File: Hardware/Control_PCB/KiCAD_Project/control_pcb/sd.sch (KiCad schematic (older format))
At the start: 9 parts, among them J5 Micro_SD_Card_Det

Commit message: Draft of next layout
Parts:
- added C12, C13, C14, C15: 1-0000007, capacitors_0603:1-0000007, symbol capacitors_0603:1-0000007
- added D6: Activity, LED_SMD:LED_0805_2012Metric, symbol Device:LED
- added D7: Error, LED_SMD:LED_0805_2012Metric, symbol Device:LED
- added J7: SD_uC_ISP, Connector_PinHeader_2.54mm:PinHeader_2x03_P2.54mm_Vertical, symbol Connector_Generic:Conn_02x03_Odd_Even
- added R25: 1-0000010, resistors_0603:1-0000010, symbol resistors_0603:1-0000010
- added R26, R27: 1-0000006, resistors_0603:1-0000006, symbol resistors_0603:1-0000006
- added R28, R36: 150, Resistor_SMD:R_0603_1608Metric, symbol Device:R
- added U4: ATmega328P-AU, Package_QFP:TQFP-32_7x7mm_P0.8mm, symbol lib_sch:ATmega328P-AU
- added Y3: 16MHz, lib_fp:Resonator, symbol Device:Resonator_Small
- C16: renamed from C11; footprint Capacitors_SMD:C_0603_HandSoldering -> Capacitor_SMD:C_0603_1608Metric
- R29: renamed from R11; footprint Resistors_SMD:R_0603_HandSoldering -> Resistor_SMD:R_0603_1608Metric
- R30: renamed from R12; footprint Resistors_SMD:R_0603_HandSoldering -> Resistor_SMD:R_0603_1608Metric
- R31: renamed from R13; footprint Resistors_SMD:R_0603_HandSoldering -> Resistor_SMD:R_0603_1608Metric
- R32: renamed from R14; footprint Resistors_SMD:R_0603_HandSoldering -> Resistor_SMD:R_0603_1608Metric
- R33: renamed from R15; footprint Resistors_SMD:R_0603_HandSoldering -> Resistor_SMD:R_0603_1608Metric
- R34: renamed from R16; footprint Resistors_SMD:R_0603_HandSoldering -> Resistor_SMD:R_0603_1608Metric
- R35: renamed from R17; footprint Resistors_SMD:R_0603_HandSoldering -> Resistor_SMD:R_0603_1608Metric
- renumbered J5 to J6
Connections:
- net +3V3: now also C12.1, C13.1, C14.1, J7.2 (Pin_2), R25.1, U4.18 (AVCC), U4.4 (VCC), U4.6 (VCC)
- net GND: now also C12.2, C13.2, C14.2, C15.2, D6.1 (K), D7.1 (K), J7.6 (Pin_6), U4.21 (GND), U4.3 (GND), U4.5 (GND), Y3.2
- net SD_CS renamed SD_uC_CS
- net SD_uC_CS: now also U4.12 (PB0)
- net SD_DETECT renamed SD_uC_CD
- net SD_uC_CD: now also U4.13 (PB1)
- net SPI1_MISO renamed SD_uC_MISO
- net SD_uC_MISO: now also J7.1 (Pin_1), U4.16 (PB4)
- net SPI1_MOSI renamed SD_uC_MOSI
- net SD_uC_MOSI: now also J7.4 (Pin_4), U4.15 (PB3)
- net SPI1_SCLK renamed SD_uC_SCK
- net SD_uC_SCK: now also J7.3 (Pin_3), U4.17 (PB5)
- new net: R28.2, U4.2 (PD4)
- new net: C15.1, U4.20 (AREF)
- new net: R26.2, U4.30 (PD0)
- new net: R27.2, U4.31 (PD1)
- new net: U4.7 (XTAL1/PB6), Y3.1
- new net: U4.8 (XTAL2/PB7), Y3.3
- new net: R36.2, U4.9 (PD5)
- new net: D6.2 (A), R28.1
- new net: D7.2 (A), R36.1
- new net RX_FROM_STM: R26.1
- new net SD_uC_RESET: J7.5 (Pin_5), R25.2, U4.29 (~RESET~/PC6)
- new net TX_TO_STM: R27.1
- no-connect marks 0 -> 13
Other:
- note added: "SD uC gets the serial data stream from the STM32 and writes it all to the SD card.\nIt handles rolling the file name to the next available and then simply dumps\neverything it receives which should only be complete packets since the STM32\ntakes care of that."
- moved on the sheet: C16, J6, R29, R30, R31, R32, R33, R34, R35

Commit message: Add final production files
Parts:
- J7: Internal Part Number (none) -> 0-0000000; Populated (none) -> 0
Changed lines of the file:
@@
 Sheet 3 6
 Title "Control Paddle Electronics - NSSL EFM"
-Date "2020-03-31"
-Rev "2.0"
+Date "2020-12-30"
+Rev "3.0"
 Comp "Leeman Geophysical LLC"
 Comment1 "(479) 373-3736"
@@
 $EndComp
 $Comp
-L power:+3V3 #PWR041
+L power:+3V3 #PWR039
 U 1 1 5DEE2763
 P 8000 4375
-F 0 "#PWR041" H 8000 4225 50  0001 C CNN
+F 0 "#PWR039" H 8000 4225 50  0001 C CNN
 F 1 "+3V3" H 8015 4548 50  0000 C CNN
 F 2 "" H 8000 4375 50  0001 C CNN
@@
 	8000 5725 8000 4775
 $Comp
-L power:GND #PWR047
+L power:GND #PWR045
 U 1 1 5DEE6EC1
 P 9300 6225
-F 0 "#PWR047" H 9300 5975 50  0001 C CNN
+F 0 "#PWR045" H 9300 5975 50  0001 C CNN
 F 1 "GND" H 9305 6052 50  0000 C CNN
 F 2 "" H 9300 6225 50  0001 C CNN
@@
 $EndComp
 $Comp
-L power:GND #PWR048
+L power:GND #PWR046
 U 1 1 5DEE73D1
 P 9650 6225
-F 0 "#PWR048" H 9650 5975 50  0001 C CNN
+F 0 "#PWR046" H 9650 5975 50  0001 C CNN
 F 1 "GND" H 9655 6052 50  0000 C CNN
 F 2 "" H 9650 6225 50  0001 C CNN
@@
 $EndComp
 $Comp
-L power:GND #PWR042
+L power:GND #PWR040
 U 1 1 5DEEA7AB
 P 9600 4400
-F 0 "#PWR042" H 9600 4150 50  0001 C CNN
+F 0 "#PWR040" H 9600 4150 50  0001 C CNN
 F 1 "GND" H 9605 4227 50  0000 C CNN
 F 2 "" H 9600 4400 50  0001 C CNN
@@
 $EndComp
 $Comp
-L power:+3V3 #PWR040
+L power:+3V3 #PWR038
 U 1 1 5DEEACAB
 P 9300 4275
-F 0 "#PWR040" H 9300 4125 50  0001 C CNN
+F 0 "#PWR038" H 9300 4125 50  0001 C CNN
 F 1 "+3V3" H 9315 4448 50  0000 C CNN
 F 2 "" H 9300 4275 50  0001 C CNN
@@
 P 2925 3175
 AR Path="/5DED0CD0/5FF2D775" Ref="#PWR?"  Part="1"
-AR Path="/5DEDFC42/5FF2D775" Ref="#PWR039"  Part="1"
-F 0 "#PWR039" H 2925 2925 50  0001 C CNN
+AR Path="/5DEDFC42/5FF2D775" Ref="#PWR037"  Part="1"
+F 0 "#PWR037" H 2925 2925 50  0001 C CNN
 F 1 "GND" H 2930 3002 50  0000 C CNN
 F 2 "" H 2925 3175 50  0001 C CNN
@@
 P 3975 5275
 AR Path="/5DED0CD0/5FF2D793" Ref="#PWR?"  Part="1"
-AR Path="/5DEDFC42/5FF2D793" Ref="#PWR044"  Part="1"
-F 0 "#PWR044" H 3975 5025 50  0001 C CNN
+AR Path="/5DEDFC42/5FF2D793" Ref="#PWR042"  Part="1"
+F 0 "#PWR042" H 3975 5025 50  0001 C CNN
 F 1 "GND" H 3980 5102 50  0000 C CNN
 F 2 "" H 3975 5275 50  0001 C CNN
@@
 P 3075 2475
 AR Path="/5DED0CD0/5FF2D7A9" Ref="#PWR?"  Part="1"
-AR Path="/5DEDFC42/5FF2D7A9" Ref="#PWR038"  Part="1"
-F 0 "#PWR038" H 3075 2225 50  0001 C CNN
+AR Path="/5DEDFC42/5FF2D7A9" Ref="#PWR036"  Part="1"
+F 0 "#PWR036" H 3075 2225 50  0001 C CNN
 F 1 "GND" H 3080 2302 50  0000 C CNN
 F 2 "" H 3075 2475 50  0001 C CNN
@@
 P 3975 1375
 AR Path="/5DED0CD0/5FF2D7E6" Ref="#PWR?"  Part="1"
-AR Path="/5DEDFC42/5FF2D7E6" Ref="#PWR035"  Part="1"
-F 0 "#PWR035" H 3975 1225 50  0001 C CNN
+AR Path="/5DEDFC42/5FF2D7E6" Ref="#PWR033"  Part="1"
+F 0 "#PWR033" H 3975 1225 50  0001 C CNN
 F 1 "+3V3" H 3990 1548 50  0000 C CNN
 F 2 "" H 3975 1375 50  0001 C CNN
@@
 P 3250 2025
 AR Path="/5DED0CD0/5FF2D7EC" Ref="#PWR?"  Part="1"
-AR Path="/5DEDFC42/5FF2D7EC" Ref="#PWR036"  Part="1"
-F 0 "#PWR036" H 3250 1775 50  0001 C CNN
+AR Path="/5DEDFC42/5FF2D7EC" Ref="#PWR034"  Part="1"
+F 0 "#PWR034" H 3250 1775 50  0001 C CNN
 F 1 "GND" H 3100 1950 50  0000 C CNN
 F 2 "" H 3250 2025 50  0001 C CNN
@@
 P 2525 2400
 AR Path="/5DED0CD0/5FF2D7FA" Ref="#PWR?"  Part="1"
-AR Path="/5DEDFC42/5FF2D7FA" Ref="#PWR037"  Part="1"
-F 0 "#PWR037" H 2525 2250 50  0001 C CNN
+AR Path="/5DEDFC42/5FF2D7FA" Ref="#PWR035"  Part="1"
+F 0 "#PWR035" H 2525 2250 50  0001 C CNN
 F 1 "+3V3" H 2540 2573 50  0000 C CNN
 F 2 "" H 2525 2400 50  0001 C CNN
@@
 P 4300 5925
 AR Path="/5DED0CD0/5FF2D808" Ref="#PWR?"  Part="1"
-AR Path="/5DEDFC42/5FF2D808" Ref="#PWR045"  Part="1"
-F 0 "#PWR045" H 4300 5775 50  0001 C CNN
+AR Path="/5DEDFC42/5FF2D808" Ref="#PWR043"  Part="1"
+F 0 "#PWR043" H 4300 5775 50  0001 C CNN
 F 1 "+3V3" H 4315 6098 50  0000 C CNN
 F 2 "" H 4300 5925 50  0001 C CNN
@@
 P 4300 6125
 AR Path="/5DED0CD0/5FF2D816" Ref="#PWR?"  Part="1"
-AR Path="/5DEDFC42/5FF2D816" Ref="#PWR046"  Part="1"
-F 0 "#PWR046" H 4300 5875 50  0001 C CNN
+AR Path="/5DEDFC42/5FF2D816" Ref="#PWR044"  Part="1"
+F 0 "#PWR044" H 4300 5875 50  0001 C CNN
 F 1 "GND" H 4305 5952 50  0000 C CNN
 F 2 "" H 4300 6125 50  0001 C CNN
@@
 P 5850 4900
 AR Path="/5FFDD0BF" Ref="#PWR?"  Part="1"
-AR Path="/5DEDFC42/5FFDD0BF" Ref="#PWR043"  Part="1"
-F 0 "#PWR043" H 5850 4650 50  0001 C CNN
+AR Path="/5DEDFC42/5FFDD0BF" Ref="#PWR041"  Part="1"
+F 0 "#PWR041" H 5850 4650 50  0001 C CNN
 F 1 "GND" H 5855 4727 50  0000 C CNN
 F 2 "" H 5850 4900 50  0001 C CNN
@@
 F 2 "Connector_PinHeader_2.54mm:PinHeader_2x03_P2.54mm_Vertical" H 4000 6025 50  0001 C CNN
 F 3 "~" H 4000 6025 50  0001 C CNN
+F 4 "0-0000000" H 4000 6025 50  0001 C CNN "Internal Part Number"
+F 5 "0" H 4000 6025 50  0001 C CNN "Populated"
 	1    4000 6025
 	1    0    0    -1

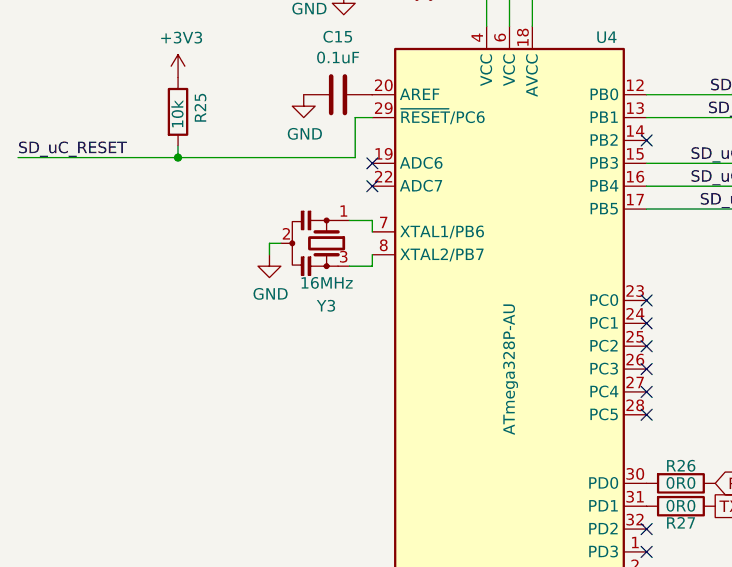
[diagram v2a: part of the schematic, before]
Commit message: Fix incorrect crystal part numbers and add production files for Rev 3.0
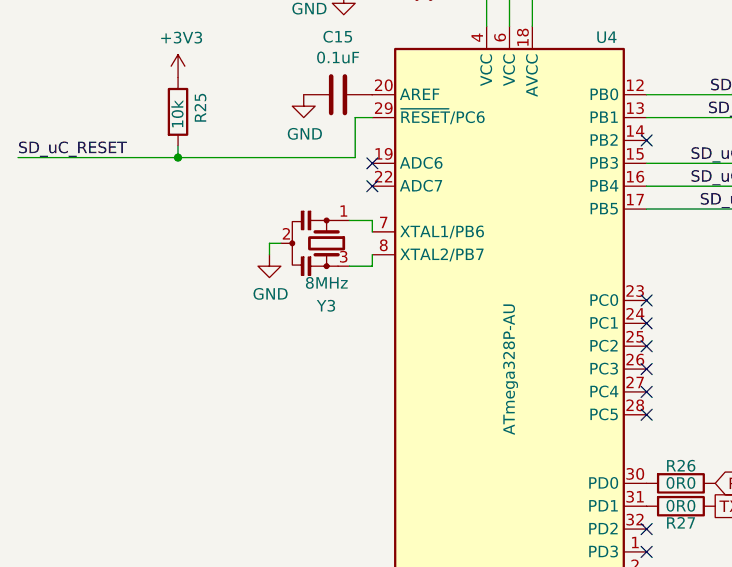
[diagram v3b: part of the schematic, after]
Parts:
- Y3: value 16MHz -> 8MHz; Internal Part Number 1-0000569 -> 1-0000721
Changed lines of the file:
@@
 AR Path="/5DEDFC42/5FF2D76B" Ref="Y3"  Part="1"
 F 0 "Y3" V 3450 3125 50  0000 C CNN
-F 1 "16MHz" V 3350 3125 50  0000 C CNN
+F 1 "8MHz" V 3350 3125 50  0000 C CNN
 F 2 "lib_fp:Resonator" H 3150 3125 50  0001 C CNN
 F 3 "~" H 3150 3125 50  0001 C CNN
-F 4 "1-0000569" H 3175 3125 50  0001 C CNN "Internal Part Number"
+F 4 "1-0000721" H 3175 3125 50  0001 C CNN "Internal Part Number"
 F 5 "1" H 3175 3125 50  0001 C CNN "Populated"
 	1    3175 3125

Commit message: Control Rev 3.1
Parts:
- D6, D7: footprint LED_SMD:LED_0805_2012Metric -> LED_THT:LED_D3.0mm_Horizontal_O1.27mm_Z2.0mm_Clear
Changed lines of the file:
@@
 Sheet 3 6
 Title "Control Paddle Electronics - NSSL EFM"
-Date "2020-12-30"
-Rev "3.0"
+Date "2021-11-22"
+Rev "3.1"
 Comp "Leeman Geophysical LLC"
 Comment1 "(479) 373-3736"
@@
 F 0 "D6" H 5618 4320 50  0000 C CNN
 F 1 "Activity" H 5618 4411 50  0000 C CNN
-F 2 "LED_SMD:LED_0805_2012Metric" H 5625 4575 50  0001 C CNN
+F 2 "LED_THT:LED_D3.0mm_Horizontal_O1.27mm_Z2.0mm_Clear" H 5625 4575 50  0001 C CNN
 F 3 "~" H 5625 4575 50  0001 C CNN
 F 4 "1-0000599" H 5625 4575 50  0001 C CNN "Internal Part Number"
@@
 F 0 "D7" H 5625 5000 50  0000 C CNN
 F 1 "Error" H 5625 4900 50  0000 C CNN
-F 2 "LED_SMD:LED_0805_2012Metric" H 5625 4800 50  0001 C CNN
+F 2 "LED_THT:LED_D3.0mm_Horizontal_O1.27mm_Z2.0mm_Clear" H 5625 4800 50  0001 C CNN
 F 3 "~" H 5625 4800 50  0001 C CNN
 F 4 "1-0000600" H 5625 4800 50  0001 C CNN "Internal Part Number"
